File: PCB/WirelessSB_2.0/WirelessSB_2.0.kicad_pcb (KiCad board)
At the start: 2 copper layers, 66 x 61 mm, 15 parts, among them J1 Battery, SW1 PB1(Shift), SW10 PB7(R14), SW13 PB4(GTOut), SW14 PB8(Pos), SW2 PB5(HFoul), SW3 PB9(HScore), SW4 PB13(R24), SW5 PB2(Buzzer), SW6 PB6(GFoul), SW7 PB10(GScore), SW8 PB14(StartStop), SW9 PB3(HTOut), U1 ATmega328P-A, U2 AMS1117-3.3

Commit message: Done with the Controller main PCB
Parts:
- added C1: 22pF, Capacitor_SMD:C_1206_3216Metric_Pad1.33x1.80mm_HandSolder, B.Cu at (139.6, 66.8)
- added C2: 22pF, Capacitor_SMD:C_1206_3216Metric_Pad1.33x1.80mm_HandSolder, B.Cu at (147.6, 66.8)
- added C3: 100nF, Capacitor_SMD:C_1206_3216Metric_Pad1.33x1.80mm_HandSolder, B.Cu at (122.6, 66.7)
- added C4: 100nF, Capacitor_SMD:C_1206_3216Metric_Pad1.33x1.80mm_HandSolder, F.Cu at (141.4, 74.2)
- added C5: 100nF, Capacitor_SMD:C_1206_3216Metric_Pad1.33x1.80mm_HandSolder, F.Cu at (169.1, 75.1)
- added D1: LED_ARGB, LED_THT:LED_D5.0mm-4_RGB, F.Cu at (161.7, 62.5)
- added J2: OLED Display, Connector_Harwin:Harwin_M20-89004xx_1x04_P2.54mm_Horizontal, F.Cu at (154.8, 54.9)
- added J3: FTDI Programmer, Connector_PinHeader_2.54mm:PinHeader_1x06_P2.54mm_Vertical, F.Cu at (122.6, 61.9)
- added R1: 330R, Resistor_SMD:R_1206_3216Metric_Pad1.30x1.75mm_HandSolder, B.Cu at (144.9, 81.8)
- added R2: 100R, Resistor_SMD:R_1206_3216Metric_Pad1.30x1.75mm_HandSolder, B.Cu at (139.5, 81.8)
- added R3: 1K, Resistor_SMD:R_1206_3216Metric_Pad1.30x1.75mm_HandSolder, B.Cu at (152.7, 72.0)
- added R4: 1K, Resistor_SMD:R_1206_3216Metric_Pad1.30x1.75mm_HandSolder, B.Cu at (133.7, 72.1)
- added REF**: MountingHole_4.3mm_M4_ISO7380, MountingHole:MountingHole_4.3mm_M4_ISO7380, F.Cu at (113.7, 112.7)
- added REF**: MountingHole_4.3mm_M4_ISO7380, MountingHole:MountingHole_4.3mm_M4_ISO7380, F.Cu at (142.1, 97.5)
- added REF**: MountingHole_4.3mm_M4_ISO7380, MountingHole:MountingHole_4.3mm_M4_ISO7380, F.Cu at (171.2, 112.6)
- added REF**: MountingHole_4.3mm_M4_ISO7380, MountingHole:MountingHole_4.3mm_M4_ISO7380, F.Cu at (171.1, 63.0)
- added REF**: MountingHole_4.3mm_M4_ISO7380, MountingHole:MountingHole_4.3mm_M4_ISO7380, F.Cu at (113.5, 63.5)
- added REF**: KiCad-Logo2_5mm_SilkScreen, Symbol:KiCad-Logo2_5mm_SilkScreen, F.Cu at (126.0, 97.5)
- added U3: NRF24L01_Breakout, mysensors_radios:NRF24L01-SMD, F.Cu at (120.6, 75.0)
- added Y1: Crystal, Crystal:Crystal_HC18-U_Vertical, F.Cu at (146.1, 64.3)
- J1: value Battery -> Battery+Switch; footprint Connector_PinHeader_1.27mm:PinHeader_1x02_P1.27mm_Vertical_SMD_Pin1Left -> Connector_Harwin:Harwin_M20-89003xx_1x03_P2.54mm_Horizontal; moved to F.Cu
- moved J1 55.0 mm to (179.4, 75.1), turned to 0 degrees
- moved U1 48.9 mm to (141.1, 74.0), turned to -90 degrees
- moved SW1 42.0 mm to (116.2, 87.8)
- moved SW3 42.0 mm to (116.2, 102.8)
- moved SW7 42.0 mm to (116.2, 117.8)
- moved SW10 42.0 mm to (131.2, 87.8)
- moved SW13 42.0 mm to (146.2, 117.8)
- moved SW14 42.0 mm to (161.2, 102.8)
- moved SW2 42.0 mm to (131.2, 102.8)
- moved SW4 42.0 mm to (146.2, 87.8)
- moved SW5 42.0 mm to (161.2, 87.8)
- moved SW6 42.0 mm to (131.2, 117.8)
- moved SW8 42.0 mm to (161.2, 117.8)
- moved SW9 42.0 mm to (146.2, 102.8)
- moved U2 27.3 mm to (122.8, 82.3), turned to -90 degrees
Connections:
- J1 pad 2: GND -> unconnected-(J1-Pad2)
- U1 pad 10: unconnected-(U1-Pad10) -> Net-(U1-Pad10)
- U1 pad 11: unconnected-(U1-Pad11) -> LED_RGB_R
- U1 pad 12: unconnected-(U1-Pad12) -> LED_RGB_G
- U1 pad 13: unconnected-(U1-Pad13) -> NCE
- U1 pad 14: unconnected-(U1-Pad14) -> CSN
- U1 pad 15: unconnected-(U1-Pad15) -> MOSI
- U1 pad 16: unconnected-(U1-Pad16) -> MISO
- U1 pad 17: unconnected-(U1-Pad17) -> SCK
- U1 pad 18: unconnected-(U1-Pad18) -> VCC
- U1 pad 19: unconnected-(U1-Pad19) -> Net-(U1-Pad19)
- U1 pad 20: unconnected-(U1-Pad20) -> Net-(U1-Pad20)
- U1 pad 22: unconnected-(U1-Pad22) -> LED_RGB_B
- U1 pad 27: unconnected-(U1-Pad27) -> SDA
- U1 pad 28: unconnected-(U1-Pad28) -> SCL
- U1 pad 29: unconnected-(U1-Pad29) -> DTR
- U1 pad 30: unconnected-(U1-Pad30) -> FTDI_TX
- U1 pad 31: unconnected-(U1-Pad31) -> FTDI_RX
- U1 pad 4: Net-(U1-Pad4) -> VCC
- U1 pad 6: Net-(U1-Pad4) -> VCC
- U1 pad 7: unconnected-(U1-Pad7) -> Net-(U1-Pad7)
- U1 pad 8: unconnected-(U1-Pad8) -> Net-(U1-Pad8)
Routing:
- net SW_R2: track 0.00 -> 180.0 mm, vias 0 -> 1
- net VCC: track 0.00 -> 171.6 mm, vias 0 -> 7
- net SW_R1: track 0.00 -> 147.0 mm, vias 0 -> 4
- net GND: track 0.00 -> 140.8 mm, vias 0 -> 8
- net SW_C4: track 0.00 -> 135.9 mm, vias 0 -> 1
- net SW_C2: track 0.00 -> 114.2 mm, vias 0 -> 1
- net SW_R3: track 0.00 -> 90.4 mm, vias 0 -> 1
- net SW_C1: track 0.00 -> 75.1 mm
- net SW_R4: track 0.00 -> 69.9 mm
- net SCL: track 0.00 -> 66.1 mm, vias 0 -> 1
- net SDA: track 0.00 -> 66.0 mm, vias 0 -> 1
- net Net-(U1-Pad19): track 0.00 -> 58.9 mm, vias 0 -> 2
- net LED_RGB_B: track 0.00 -> 52.9 mm, vias 0 -> 2
- net SW_C3: track 0.00 -> 46.0 mm
- net NCE: track 0.00 -> 31.9 mm, vias 0 -> 3
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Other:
- board size 66 x 61 mm -> 66 x 68.2 mm
- board text added: "Designed By: Kenny Neutron"
- board text added: "PROfessional TECHnology"
- board text added: "ProTECH"

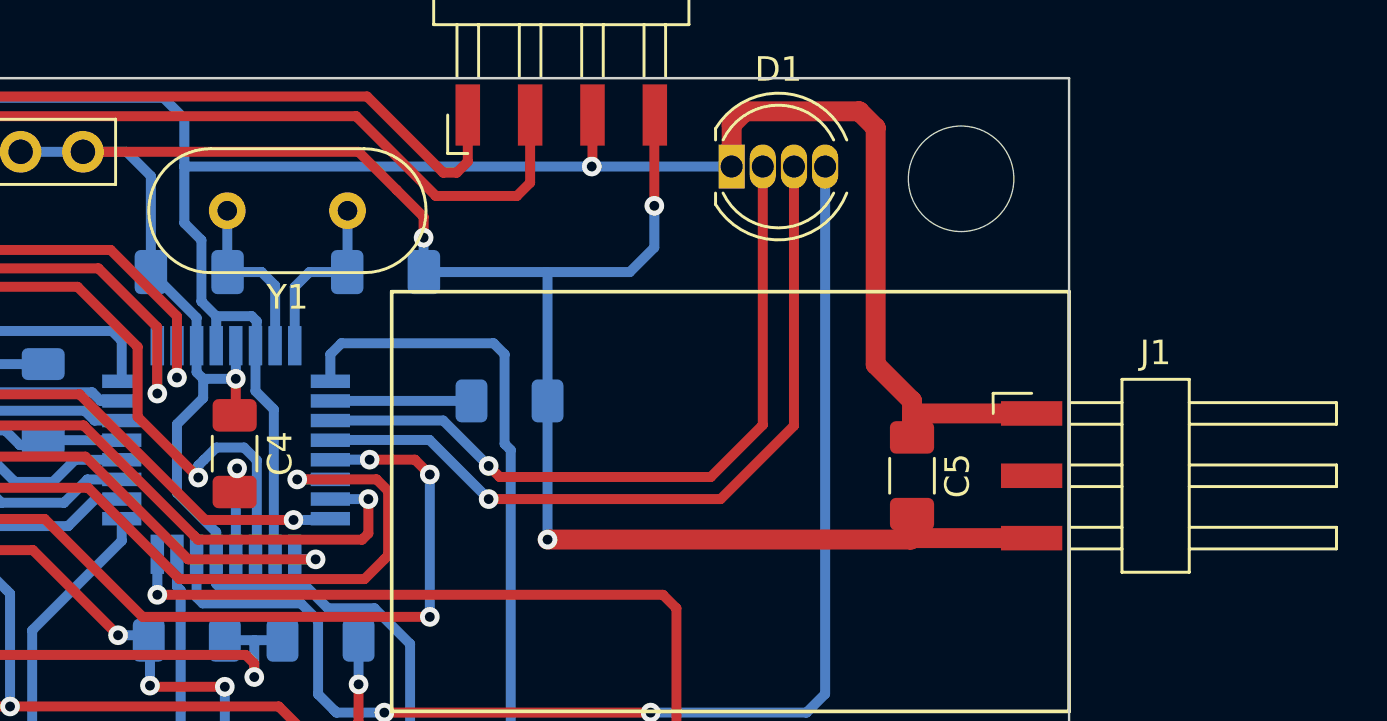
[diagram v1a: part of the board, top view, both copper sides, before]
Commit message: FIXED: moved the BatteryIN & Capacitor to the bottom layer as it hits the charge controller
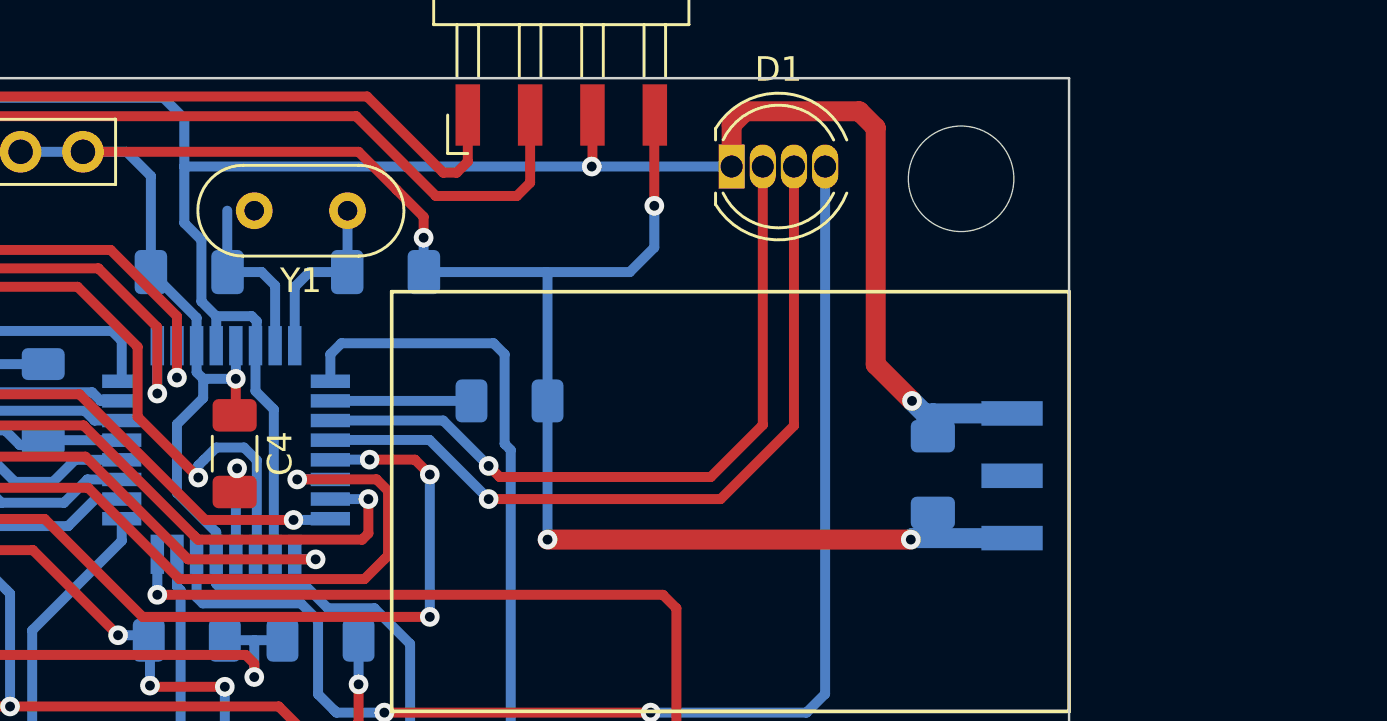
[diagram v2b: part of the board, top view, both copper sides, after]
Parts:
- C5, J1: moved to B.Cu
- Y1: footprint Crystal:Crystal_HC18-U_Vertical -> Crystal:Crystal_HC52-6mm_Vertical
- moved C5 0.85 mm to (169.9, 75.0)
- moved J1 0.80 mm to (178.7, 75.1)
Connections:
- J1 pad 1: VCC -> GND
- J1 pad 3: GND -> VCC
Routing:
- net VCC: track 171.6 -> 169.5 mm, vias 7 -> 8
- net GND: track 140.8 -> 139.0 mm, vias 8 -> 9

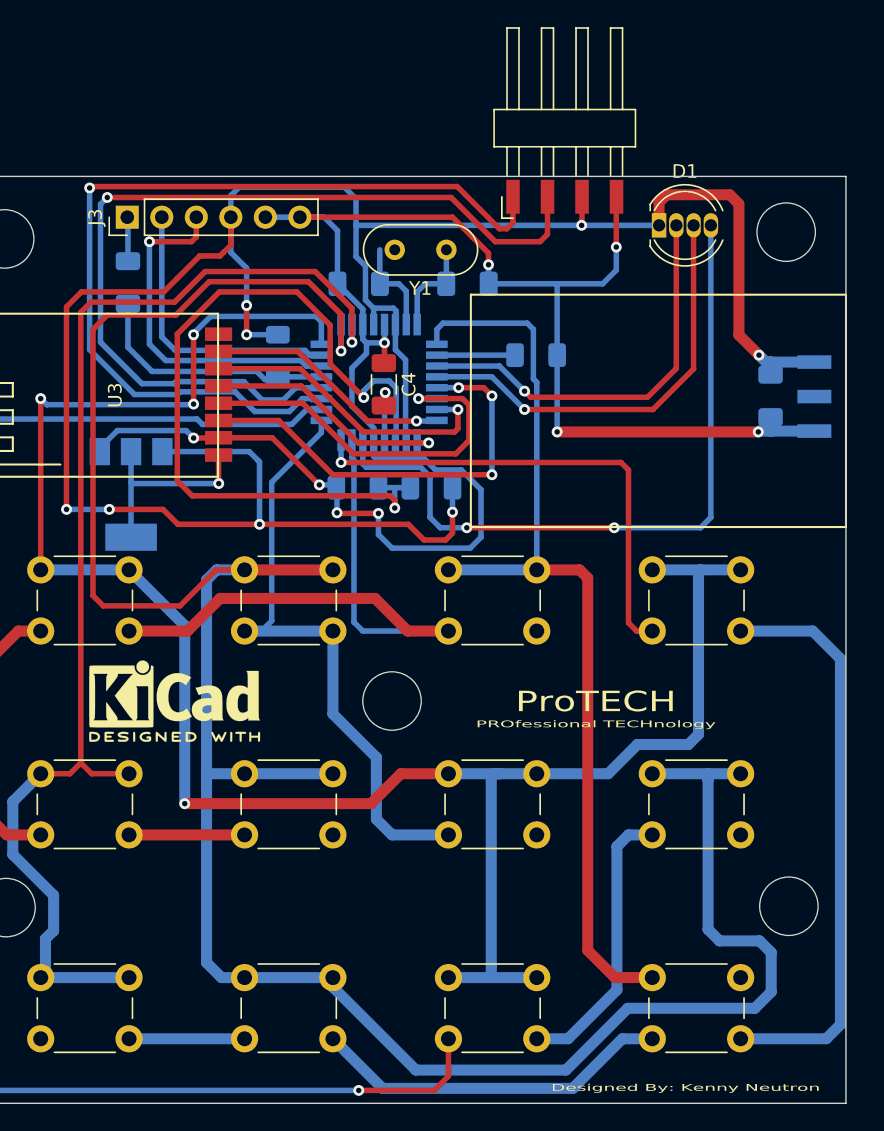
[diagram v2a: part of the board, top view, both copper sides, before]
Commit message: ADJUSTED: schematic diagram (ocd things :D) and ADDED: pdf file of the schematic from KiCAD
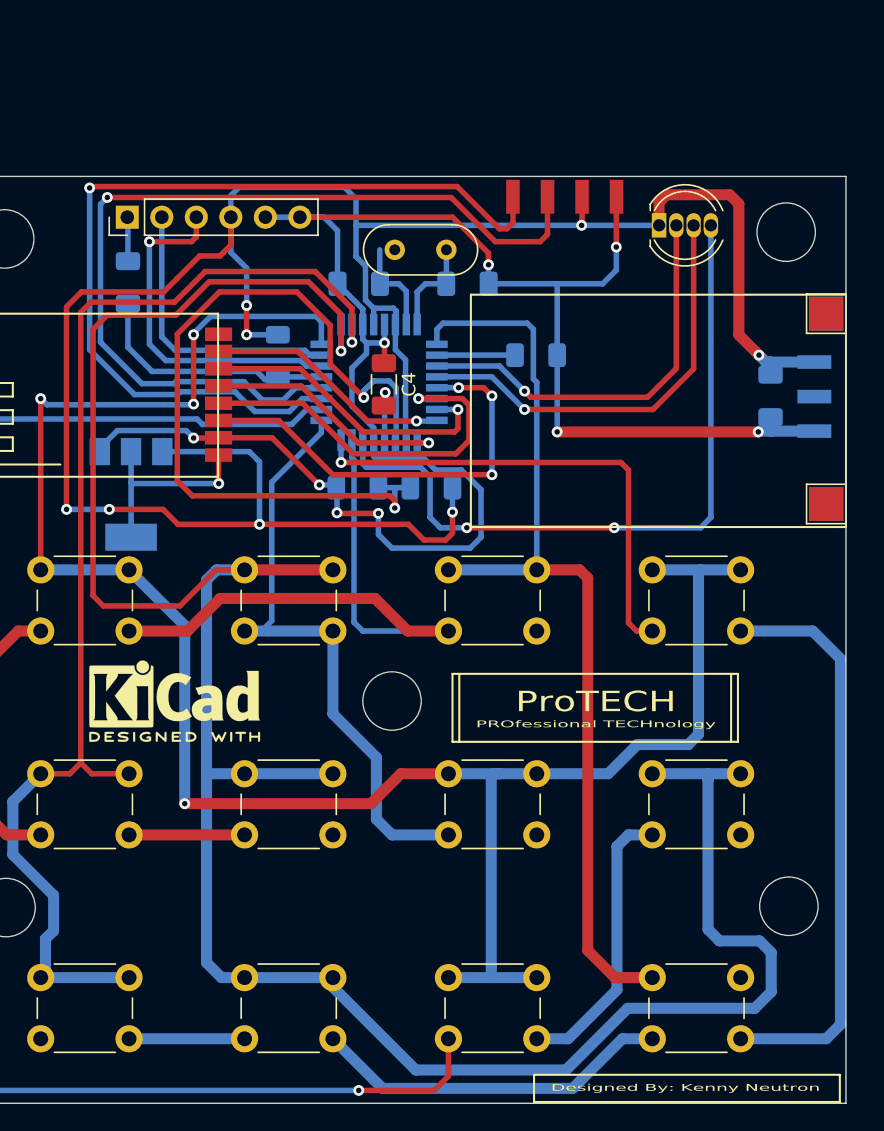
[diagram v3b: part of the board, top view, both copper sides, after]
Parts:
- added REF**: FCC-Logo_7.3x6mm_SilkScreen, Symbol:FCC-Logo_7.3x6mm_SilkScreen, B.Cu at (164.5, 82.5)
- added REF**: TestPoint_Pad_2.5x2.5mm, TestPoint:TestPoint_Pad_2.5x2.5mm, B.Cu at (174.0, 83.0)
- added REF**: TestPoint_Pad_2.5x2.5mm, TestPoint:TestPoint_Pad_2.5x2.5mm, B.Cu at (174.0, 69.0)
- added REF**: UKCA-Logo_6x6mm_SilkScreen, Symbol:UKCA-Logo_6x6mm_SilkScreen, B.Cu at (156.0, 82.5)
- added REF**: CE-Logo_11.2x8mm_SilkScreen, Symbol:CE-Logo_11.2x8mm_SilkScreen, B.Cu at (161.5, 74.0)
- added REF**: TestPoint_Pad_2.5x2.5mm, TestPoint:TestPoint_Pad_2.5x2.5mm, F.Cu at (174.0, 69.0)
- added REF**: TestPoint_Pad_2.5x2.5mm, TestPoint:TestPoint_Pad_2.5x2.5mm, F.Cu at (174.0, 83.0)
- added REF**: WEEE-Logo_4.2x6mm_SilkScreen, Symbol:WEEE-Logo_4.2x6mm_SilkScreen, B.Cu at (172.5, 123.5)
- J2: footprint Connector_Harwin:Harwin_M20-89004xx_1x04_P2.54mm_Horizontal -> Connector_Harwin:Harwin_M20-89004xx_1x04_P2.54mm_Horizontal(2)
